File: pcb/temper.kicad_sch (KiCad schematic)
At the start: 0 parts

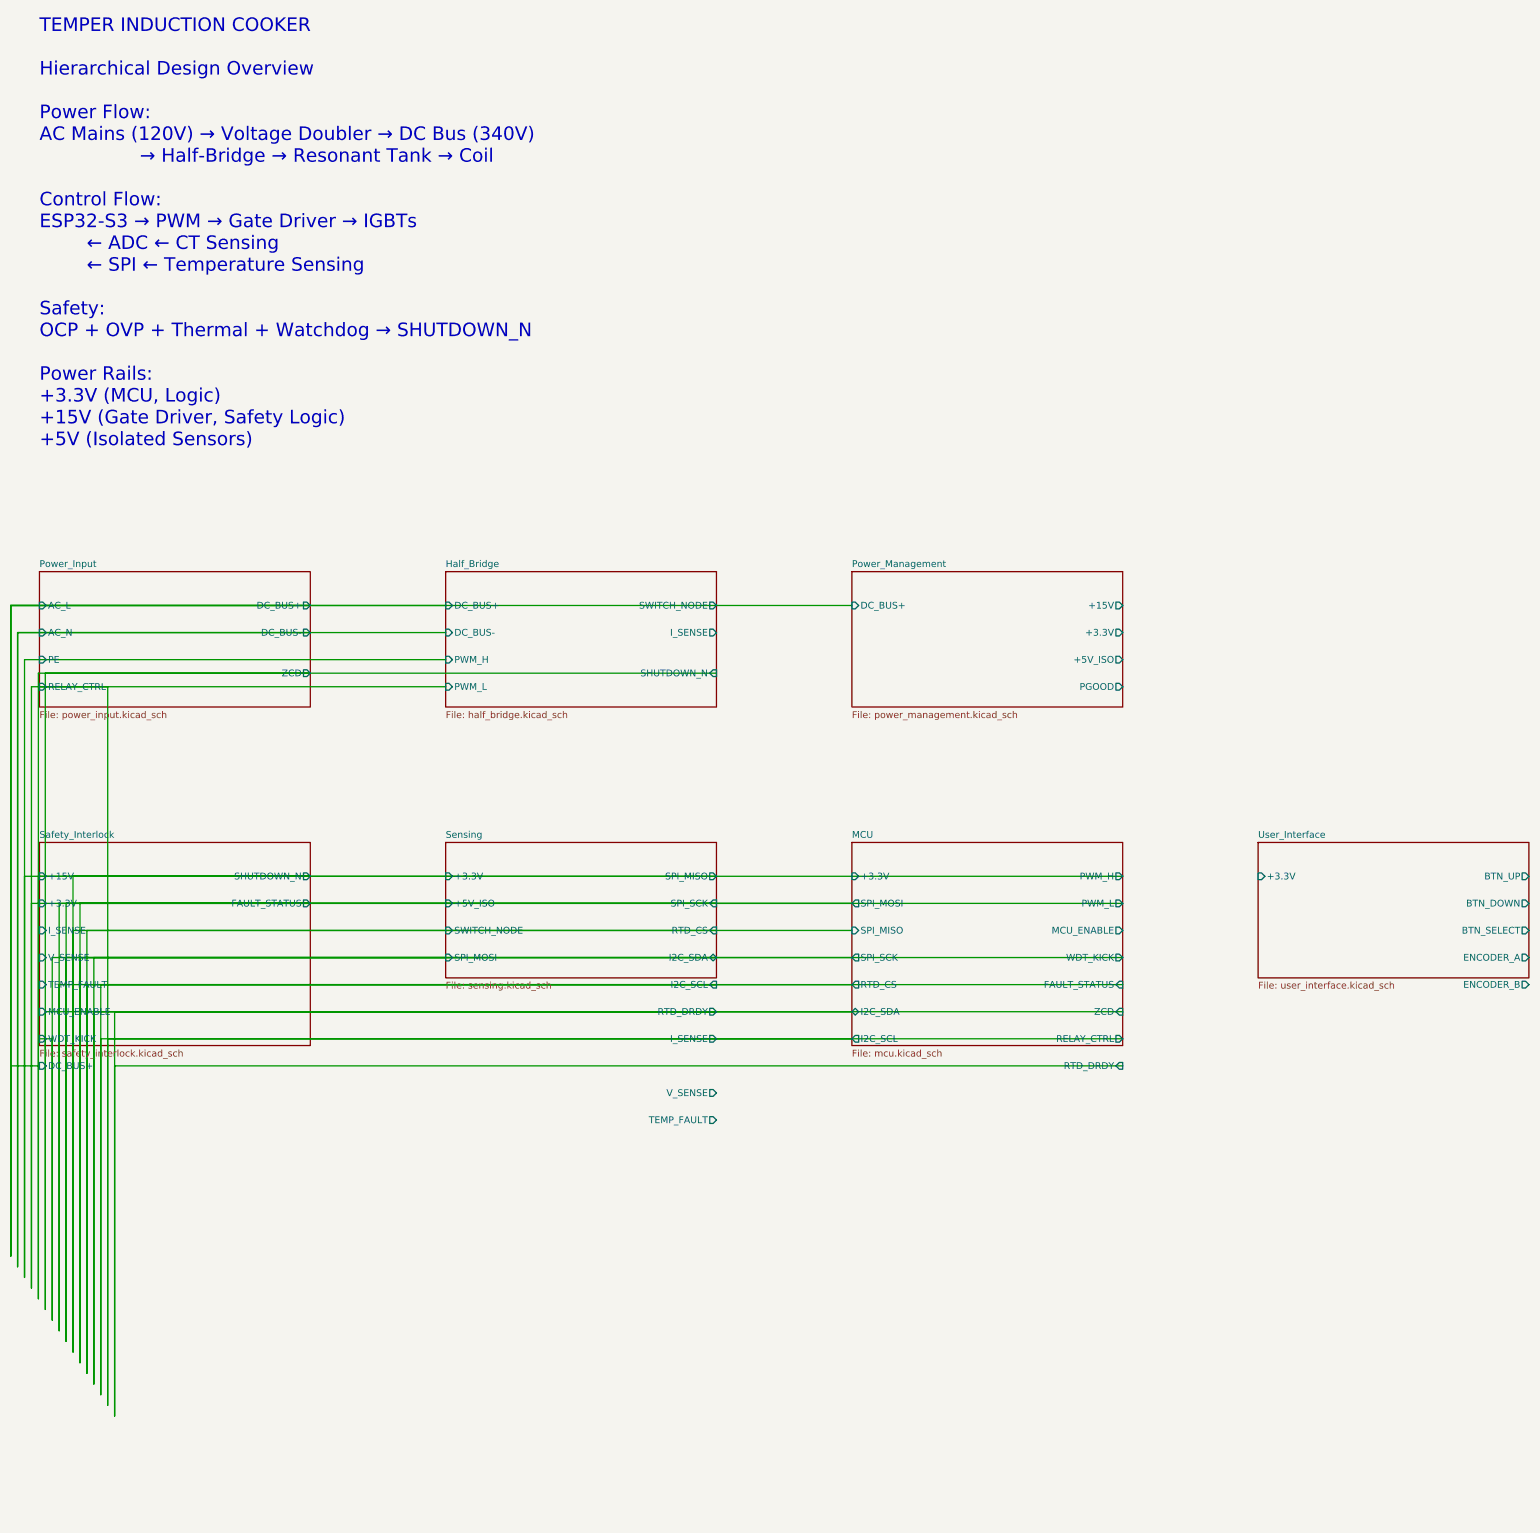
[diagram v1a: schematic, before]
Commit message: fix: remediate 8 remaining open schematic items (relay driver, R_BURDEN dedup, MAX31865 footprint, isolated 5V, RUNAWAY_CUT/RESET_N, fault-LED taps)
Closes out the open-questions list from the prior schematic repair session
(docs/plans/2026-07-14-001-fix-schematic-open-items-remediation-plan.md):

- Fix AC_N routing to the doubler's center tap (independently re-derived via
  KCL before editing mains wiring), in both the schematic and elec/src
- Give GND_CENTER a real ground connection and a Y2-capacitor PE bond;
  resolved a real conflict between two hardware docs on where system
  ground lives, using the generative .ato source as an independent tiebreaker
- Add the NTC bypass relay + low-side MOSFET driver circuit for RELAY_CTRL
- Consolidate duplicate R_BURDEN into Half_Bridge; found the surviving
  copy's signal/reference pins were swapped
- Fix the MAX31865 footprint (wrong package entirely) and add the missing
  pcb/fp-lib-table
- Add the isolated +5V_ISO DC-DC supply for the I2C isolator's far side
- Remove vestigial MCU_ENABLE; wire the real RUNAWAY_CUT net using the
  74HC4075's actual datasheet-sourced gate mapping, not pin-adjacency guesses
- Fix User_Interface's stale root pins and hierarchize the four fault-LED
  taps in Safety_Interlock (all four were floating, not just WDT_FAULT)

Every unit verified via union-find connectivity trace before and after
writing, plus a full-project kicad-cli parse/ERC pass. Three bugs were
self-caught by that discipline before landing: a lib_symbols block placed
outside its container (broke the parser outright), a RESET_N direction
mismatch, and a shared-sheet-edge routing overlap -- the latter two folded
into docs/solutions/tooling-decisions/kicad-schematic-connectivity-tracer.

Co-Authored-By: Claude Sonnet 5 <noreply@anthropic.com>
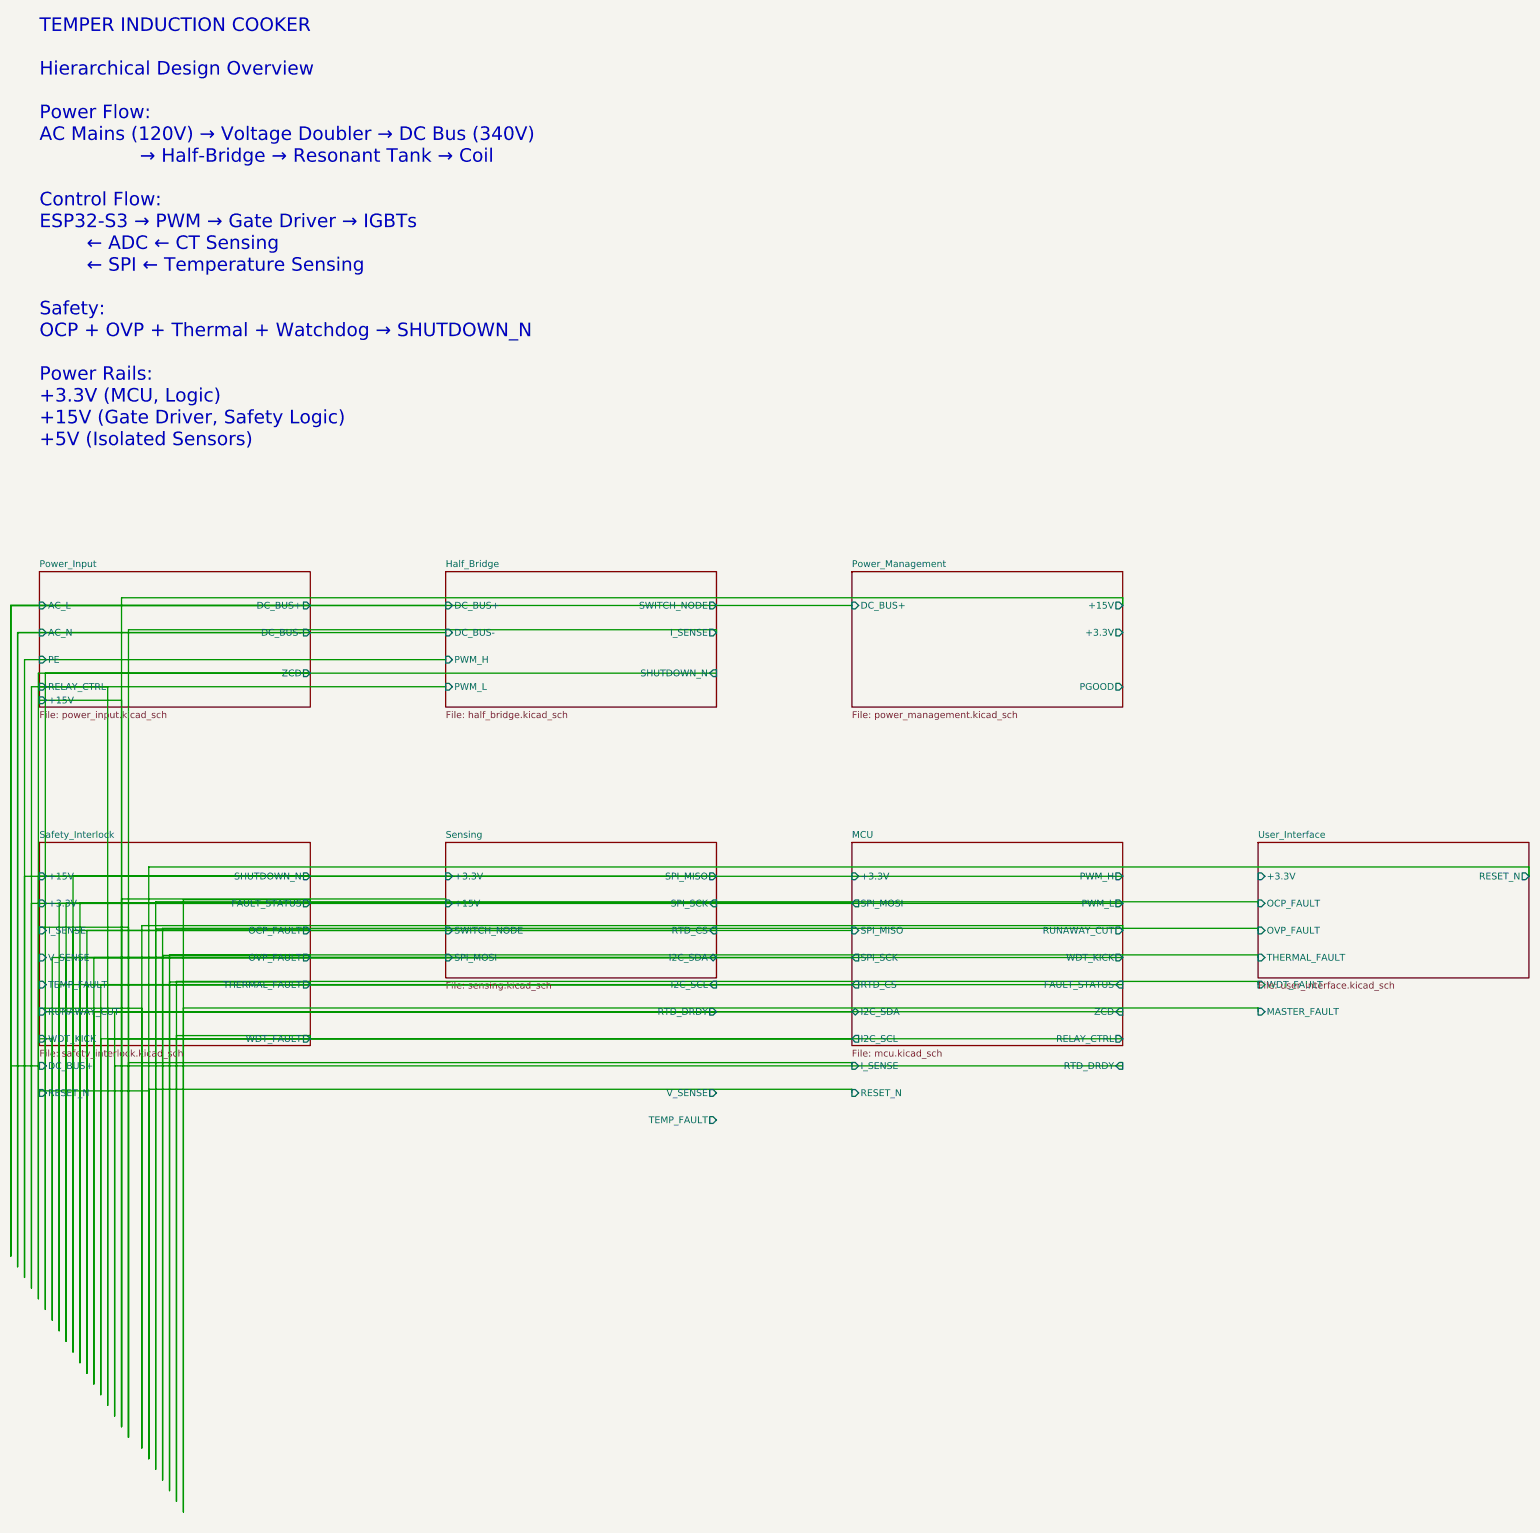
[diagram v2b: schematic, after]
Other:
- sheet MCU ports: added I_SENSE, RESET_N, RUNAWAY_CUT; removed MCU_ENABLE
- sheet Power_Input ports: added +15V; removed none
- sheet Power_Management ports: added none; removed +5V_ISO
- sheet Safety_Interlock ports: added OCP_FAULT, OVP_FAULT, RESET_N, RUNAWAY_CUT, THERMAL_FAULT, WDT_FAULT; removed MCU_ENABLE
- sheet Sensing ports: added +15V; removed +5V_ISO, I_SENSE
- sheet User_Interface ports: added MASTER_FAULT, OCP_FAULT, OVP_FAULT, RESET_N, THERMAL_FAULT, WDT_FAULT; removed BTN_DOWN, BTN_SELECT, BTN_UP, ENCODER_A, ENCODER_B
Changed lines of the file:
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@@
+      )
+    )
+    (pin "+15V" input
+      (at 25.4 125.73 180)
+      (effects
+        (font
+          (size 1.27 1.27)
+        )
+        (justify left)
       )
     )
@@
       )
     )
-    (pin "+5V_ISO" output
-      (at 228.6 118.11 0)
-      (effects
-        (font
-          (size 1.27 1.27)
-        )
-        (justify right)
-      )
-    )
     (pin "PGOOD" output
       (at 228.6 123.19 0)
@@
       )
     )
-    (pin "MCU_ENABLE" input
+    (pin "RUNAWAY_CUT" input
       (at 25.4 184.15 180)
+      (effects
+        (font
+          (size 1.27 1.27)
+        )
+        (justify left)
+      )
+    )
+    (pin "RESET_N" input
+      (at 25.4 199.39 180)
       (effects
         (font
@@
     (pin "FAULT_STATUS" output
       (at 76.2 163.83 0)
+      (effects
+        (font
+          (size 1.27 1.27)
+        )
+        (justify right)
+      )
+    )
+    (pin "OCP_FAULT" output
+      (at 76.2 168.91 0)
+      (effects
+        (font
+          (size 1.27 1.27)
+        )
+        (justify right)
+      )
+    )
+    (pin "OVP_FAULT" output
+      (at 76.2 173.99 0)
+      (effects
+        (font
+          (size 1.27 1.27)
+        )
+        (justify right)
+      )
+    )
+    (pin "THERMAL_FAULT" output
+      (at 76.2 179.07 0)
+      (effects
+        (font
+          (size 1.27 1.27)
+        )
+        (justify right)
+      )
+    )
+    (pin "WDT_FAULT" output
+      (at 76.2 189.23 0)
       (effects
         (font
@@
       )
     )
-    (pin "+5V_ISO" input
+    (pin "+15V" input
       (at 101.6 163.83 180)
       (effects
@@
     (pin "RTD_DRDY" output
       (at 152.4 184.15 0)
-      (effects
-        (font
-          (size 1.27 1.27)
-        )
-        (justify right)
-      )
-    )
-    (pin "I_SENSE" output
-      (at 152.4 189.23 0)
       (effects
         (font
@@
       )
     )
-    (pin "MCU_ENABLE" output
+    (pin "RUNAWAY_CUT" output
       (at 228.6 168.91 0)
       (effects
@@
         )
         (justify right)
+      )
+    )
+    (pin "I_SENSE" input
+      (at 177.8 194.31 180)
+      (effects
+        (font
+          (size 1.27 1.27)
+        )
+        (justify left)
+      )
+    )
+    (pin "RESET_N" input
+      (at 177.8 199.39 180)
+      (effects
+        (font
+          (size 1.27 1.27)
+        )
+        (justify left)
       )
     )
@@
       )
     )
-    (pin "BTN_UP" output
+    (pin "OCP_FAULT" input
+      (at 254 163.83 180)
+      (effects
+        (font
+          (size 1.27 1.27)
+        )
+        (justify left)
+      )
+    )
+    (pin "OVP_FAULT" input
+      (at 254 168.91 180)
+      (effects
+        (font
+          (size 1.27 1.27)
+        )
+        (justify left)
+      )
+    )
+    (pin "THERMAL_FAULT" input
+      (at 254 173.99 180)
+      (effects
+        (font
+          (size 1.27 1.27)
+        )
+        (justify left)
+      )
+    )
+    (pin "WDT_FAULT" input
+      (at 254 179.07 180)
+      (effects
+        (font
+          (size 1.27 1.27)
+        )
+        (justify left)
+      )
+    )
+    (pin "MASTER_FAULT" input
+      (at 254 184.15 180)
+      (effects
+        (font
+          (size 1.27 1.27)
+        )
+        (justify left)
+      )
+    )
+    (pin "RESET_N" output
       (at 304.8 158.75 0)
-      (effects
-        (font
-          (size 1.27 1.27)
-        )
-        (justify right)
-      )
-    )
-    (pin "BTN_DOWN" output
-      (at 304.8 163.83 0)
-      (effects
-        (font
-          (size 1.27 1.27)
-        )
-        (justify right)
-      )
-    )
-    (pin "BTN_SELECT" output
-      (at 304.8 168.91 0)
-      (effects
-        (font
-          (size 1.27 1.27)
-        )
-        (justify right)
-      )
-    )
-    (pin "ENCODER_A" output
-      (at 304.8 173.99 0)
-      (effects
-        (font
-          (size 1.27 1.27)
-        )
-        (justify right)
-      )
-    )
-    (pin "ENCODER_B" output
-      (at 304.8 179.07 0)
       (effects
         (font
@@
   (wire (pts (xy 228.6 194.31) (xy 39.5 194.31)) (stroke (width 0) (type default)))
   (wire (pts (xy 39.5 194.31) (xy 39.5 260.0)) (stroke (width 0) (type default)))
+  (wire (pts (xy 228.6 107.95) (xy 228.6 106.5)) (stroke (width 0) (type default)))
+  (wire (pts (xy 228.6 106.5) (xy 40.8 106.5)) (stroke (width 0) (type default)))
+  (wire (pts (xy 40.8 106.5) (xy 40.8 262.0)) (stroke (width 0) (type default)))
+  (wire (pts (xy 25.4 125.73) (xy 40.8 125.73)) (stroke (width 0) (type default)))
+  (wire (pts (xy 40.8 125.73) (xy 40.8 262.0)) (stroke (width 0) (type default)))
+  (wire (pts (xy 152.4 113.03) (xy 152.4 112.5)) (stroke (width 0) (type default)))
+  (wire (pts (xy 152.4 112.5) (xy 42.1 112.5)) (stroke (width 0) (type default)))
+  (wire (pts (xy 42.1 112.5) (xy 42.1 264.0)) (stroke (width 0) (type default)))
+  (wire (pts (xy 25.4 168.91) (xy 25.4 168.3)) (stroke (width 0) (type default)))
+  (wire (pts (xy 25.4 168.3) (xy 42.1 168.3)) (stroke (width 0) (type default)))
+  (wire (pts (xy 42.1 168.3) (xy 42.1 264.0)) (stroke (width 0) (type default)))
+  (wire (pts (xy 177.8 194.31) (xy 177.8 193.7)) (stroke (width 0) (type default)))
+  (wire (pts (xy 177.8 193.7) (xy 42.1 193.7)) (stroke (width 0) (type default)))
+  (wire (pts (xy 42.1 193.7) (xy 42.1 264.0)) (stroke (width 0) (type default)))
+  (wire (pts (xy 101.6 163.83) (xy 101.6 163.0)) (stroke (width 0) (type default)))
+  (wire (pts (xy 101.6 163.0) (xy 40.8 163.0)) (stroke (width 0) (type default)))
+  (wire (pts (xy 40.8 163.0) (xy 40.8 262.0)) (stroke (width 0) (type default)))
+  (wire (pts (xy 228.6 168.91) (xy 228.6 168.0)) (stroke (width 0) (type default)))
+  (wire (pts (xy 228.6 168.0) (xy 44.6 168.0)) (stroke (width 0) (type default)))
+  (wire (pts (xy 44.6 168.0) (xy 44.6 266.0)) (stroke (width 0) (type default)))
+  (wire (pts (xy 25.4 184.15) (xy 25.4 183.5)) (stroke (width 0) (type default)))
+  (wire (pts (xy 25.4 183.5) (xy 44.6 183.5)) (stroke (width 0) (type default)))
+  (wire (pts (xy 44.6 183.5) (xy 44.6 266.0)) (stroke (width 0) (type default)))
+  (wire (pts (xy 177.8 199.39) (xy 177.8 198.7)) (stroke (width 0) (type default)))
+  (wire (pts (xy 177.8 198.7) (xy 45.9 198.7)) (stroke (width 0) (type default)))
+  (wire (pts (xy 45.9 198.7) (xy 45.9 268.0)) (stroke (width 0) (type default)))
+  (wire (pts (xy 25.4 199.39) (xy 25.4 199.0)) (stroke (width 0) (type default)))
+  (wire (pts (xy 25.4 199.0) (xy 45.9 199.0)) (stroke (width 0) (type default)))
+  (wire (pts (xy 45.9 199.0) (xy 45.9 268.0)) (stroke (width 0) (type default)))
+  (wire (pts (xy 304.8 158.75) (xy 304.8 157.0)) (stroke (width 0) (type default)))
+  (wire (pts (xy 304.8 157.0) (xy 45.9 157.0)) (stroke (width 0) (type default)))
+  (wire (pts (xy 45.9 157.0) (xy 45.9 268.0)) (stroke (width 0) (type default)))
+  (wire (pts (xy 76.2 168.91) (xy 76.2 168.61)) (stroke (width 0) (type default)))
+  (wire (pts (xy 76.2 168.61) (xy 47.2 168.61)) (stroke (width 0) (type default)))
+  (wire (pts (xy 47.2 168.61) (xy 47.2 270.0)) (stroke (width 0) (type default)))
+  (wire (pts (xy 254 163.83) (xy 254 163.53)) (stroke (width 0) (type default)))
+  (wire (pts (xy 254 163.53) (xy 47.2 163.53)) (stroke (width 0) (type default)))
+  (wire (pts (xy 47.2 163.53) (xy 47.2 270.0)) (stroke (width 0) (type default)))
+  (wire (pts (xy 76.2 173.99) (xy 76.2 173.59)) (stroke (width 0) (type default)))
+  (wire (pts (xy 76.2 173.59) (xy 48.5 173.59)) (stroke (width 0) (type default)))
+  (wire (pts (xy 48.5 173.59) (xy 48.5 272.0)) (stroke (width 0) (type default)))
+  (wire (pts (xy 254 168.91) (xy 254 168.51)) (stroke (width 0) (type default)))
+  (wire (pts (xy 254 168.51) (xy 48.5 168.51)) (stroke (width 0) (type default)))
+  (wire (pts (xy 48.5 168.51) (xy 48.5 272.0)) (stroke (width 0) (type default)))
+  (wire (pts (xy 76.2 179.07) (xy 76.2 178.57)) (stroke (width 0) (type default)))
+  (wire (pts (xy 76.2 178.57) (xy 49.8 178.57)) (stroke (width 0) (type default)))
+  (wire (pts (xy 49.8 178.57) (xy 49.8 274.0)) (stroke (width 0) (type default)))
+  (wire (pts (xy 254 173.99) (xy 254 173.49)) (stroke (width 0) (type default)))
+  (wire (pts (xy 254 173.49) (xy 49.8 173.49)) (stroke (width 0) (type default)))
+  (wire (pts (xy 49.8 173.49) (xy 49.8 274.0)) (stroke (width 0) (type default)))
+  (wire (pts (xy 76.2 189.23) (xy 76.2 188.63)) (stroke (width 0) (type default)))
+  (wire (pts (xy 76.2 188.63) (xy 51.1 188.63)) (stroke (width 0) (type default)))
+  (wire (pts (xy 51.1 188.63) (xy 51.1 276.0)) (stroke (width 0) (type default)))
+  (wire (pts (xy 254 179.07) (xy 254 178.47)) (stroke (width 0) (type default)))
+  (wire (pts (xy 254 178.47) (xy 51.1 178.47)) (stroke (width 0) (type default)))
+  (wire (pts (xy 51.1 178.47) (xy 51.1 276.0)) (stroke (width 0) (type default)))
+  (wire (pts (xy 76.2 163.83) (xy 76.2 163.13)) (stroke (width 0) (type default)))
+  (wire (pts (xy 76.2 163.13) (xy 52.4 163.13)) (stroke (width 0) (type default)))
+  (wire (pts (xy 52.4 163.13) (xy 52.4 278.0)) (stroke (width 0) (type default)))
+  (wire (pts (xy 254 184.15) (xy 254 183.45)) (stroke (width 0) (type default)))
+  (wire (pts (xy 254 183.45) (xy 52.4 183.45)) (stroke (width 0) (type default)))
+  (wire (pts (xy 52.4 183.45) (xy 52.4 278.0)) (stroke (width 0) (type default)))
 )
